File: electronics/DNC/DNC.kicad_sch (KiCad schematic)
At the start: 1 part

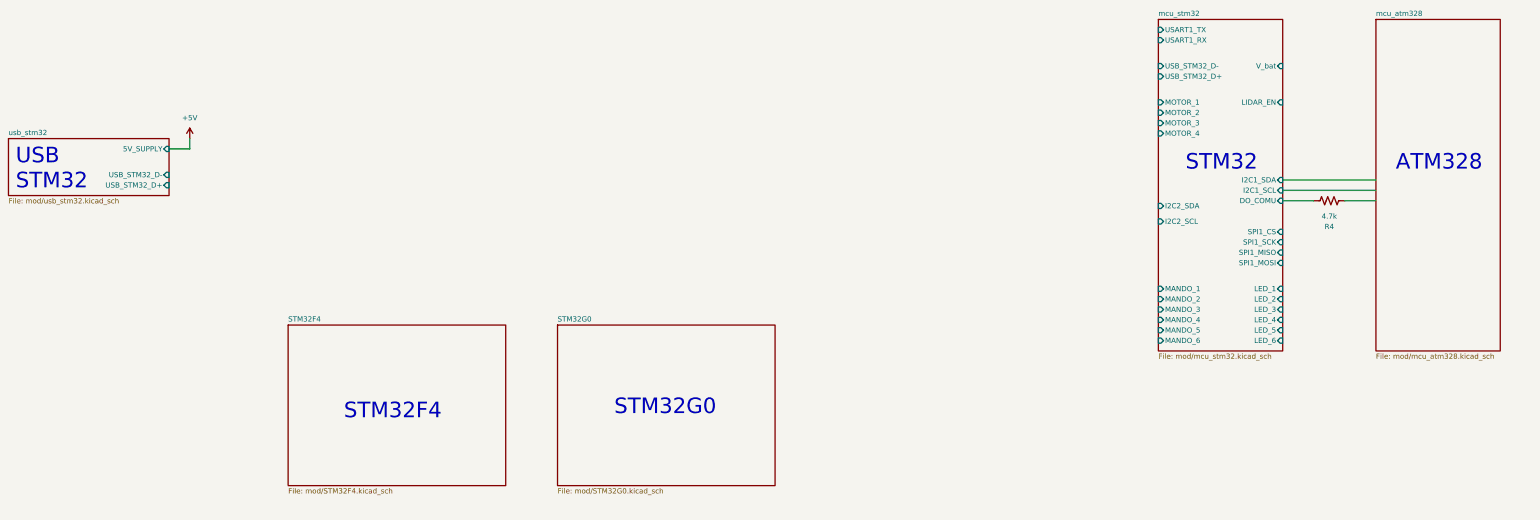
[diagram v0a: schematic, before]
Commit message: Se empezó de nuevo el diseño del DNC con una nueva arquitectura
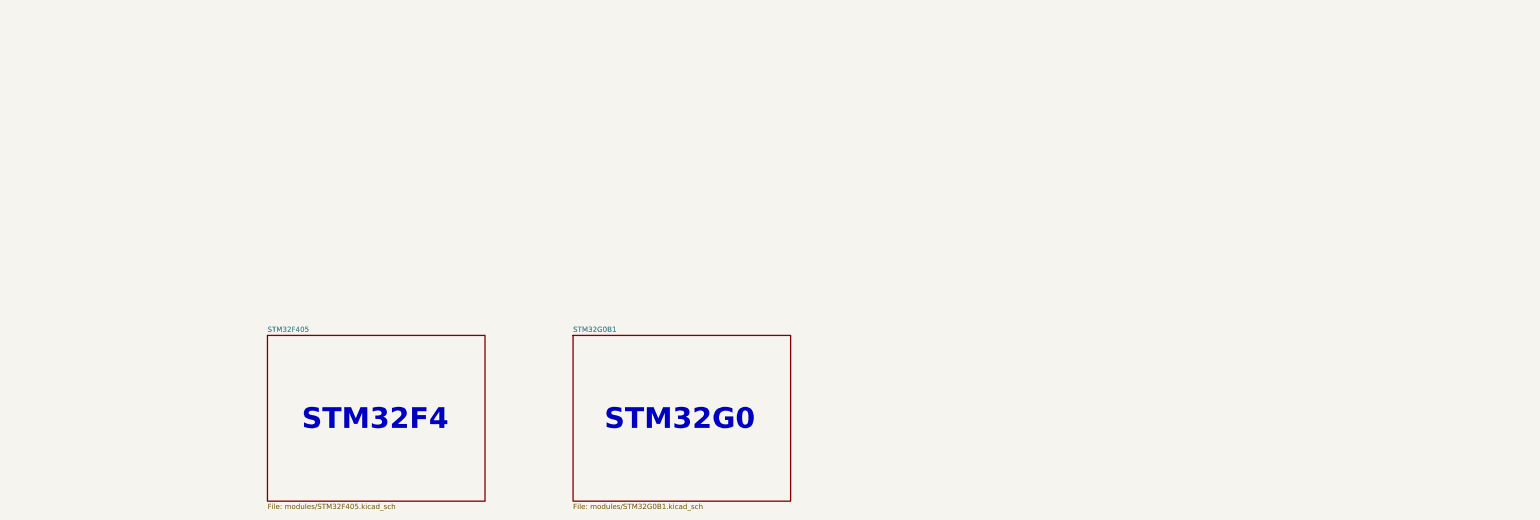
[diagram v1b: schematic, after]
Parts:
- removed R4: 4.7k, symbol Device:R_US
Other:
- removed sheet STM32F4
- removed sheet STM32G0
- removed sheet mcu_atm328
- removed sheet mcu_stm32
- removed sheet usb_stm32
- added sheet STM32F405 (modules/STM32F405.kicad_sch)
- added sheet STM32G0B1 (modules/STM32G0B1.kicad_sch)
- note removed: "ATM328"
- note removed: "STM32"
- note removed: "USB STM32"
